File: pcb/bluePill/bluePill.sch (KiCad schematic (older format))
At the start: 6 parts, among them U1 BluePill

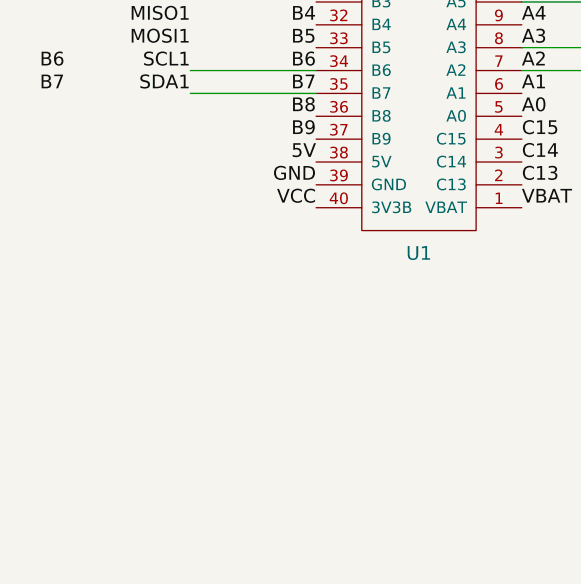
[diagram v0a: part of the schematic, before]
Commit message: Finished the Blue Pill module.
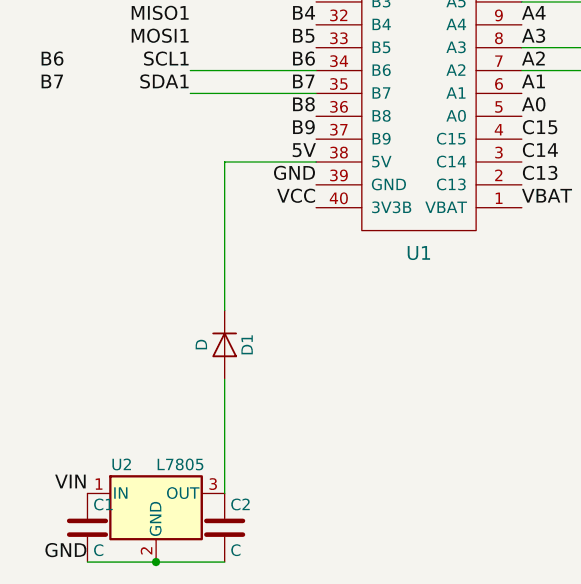
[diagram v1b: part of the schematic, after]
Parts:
- added C1, C2: C, Capacitors_THT:CP_Radial_D6.3mm_P2.50mm, symbol C
- added D1: D, Diodes_THT:D_T-1_P5.08mm_Horizontal, symbol D
- added U2: L7805, Power_Integrations:TO-220, symbol L7805
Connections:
- net 5V: now also D1.1 (K)
- net GND: now also C1.2, C2.2, U2.2 (GND)
- net VIN: now also C1.1, U2.1 (IN)
- new net: C2.1, D1.2 (A), U2.3 (OUT)
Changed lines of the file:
@@
 Text Label 900  1650 2    60   ~ 0
 A9
+$Comp
+L L7805 U2
+U 1 1 5ACA407A
+P 1250 4300
+F 0 "U2" H 1100 4425 50  0000 C CNN
+F 1 "L7805" H 1250 4425 50  0000 L CNN
+F 2 "Power_Integrations:TO-220" H 1275 4150 50  0001 L CIN
+F 3 "" H 1250 4250 50  0001 C CNN
+	1    1250 4300
+	1    0    0    -1
+$EndComp
+$Comp
+L C C1
+U 1 1 5ACA411D
+P 950 4450
+F 0 "C1" H 975 4550 50  0000 L CNN
+F 1 "C" H 975 4350 50  0000 L CNN
+F 2 "Capacitors_THT:CP_Radial_D6.3mm_P2.50mm" H 988 4300 50  0001 C CNN
+F 3 "" H 950 4450 50  0001 C CNN
+	1    950  4450
+	1    0    0    -1
+$EndComp
+$Comp
+L C C2
+U 1 1 5ACA4158
+P 1550 4450
+F 0 "C2" H 1575 4550 50  0000 L CNN
+F 1 "C" H 1575 4350 50  0000 L CNN
+F 2 "Capacitors_THT:CP_Radial_D6.3mm_P2.50mm" H 1588 4300 50  0001 C CNN
+F 3 "" H 1550 4450 50  0001 C CNN
+	1    1550 4450
+	1    0    0    -1
+$EndComp
+Wire Wire Line
+	950  4600 1550 4600
+Connection ~ 1250 4600
+Text Label 950  4300 2    60   ~ 0
+VIN
+Text Label 950  4600 2    60   ~ 0
+GND
+$Comp
+L D D1
+U 1 1 5ACA4326
+P 1550 3650
+F 0 "D1" H 1550 3750 50  0000 C CNN
+F 1 "D" H 1550 3550 50  0000 C CNN
+F 2 "Diodes_THT:D_T-1_P5.08mm_Horizontal" H 1550 3650 50  0001 C CNN
+F 3 "" H 1550 3650 50  0001 C CNN
+	1    1550 3650
+	0    1    1    0
+$EndComp
+Wire Wire Line
+	1550 4300 1550 3800
+Wire Wire Line
+	1550 3500 1550 2850
+Wire Wire Line
+	1550 2850 1950 2850
 $EndSCHEMATC

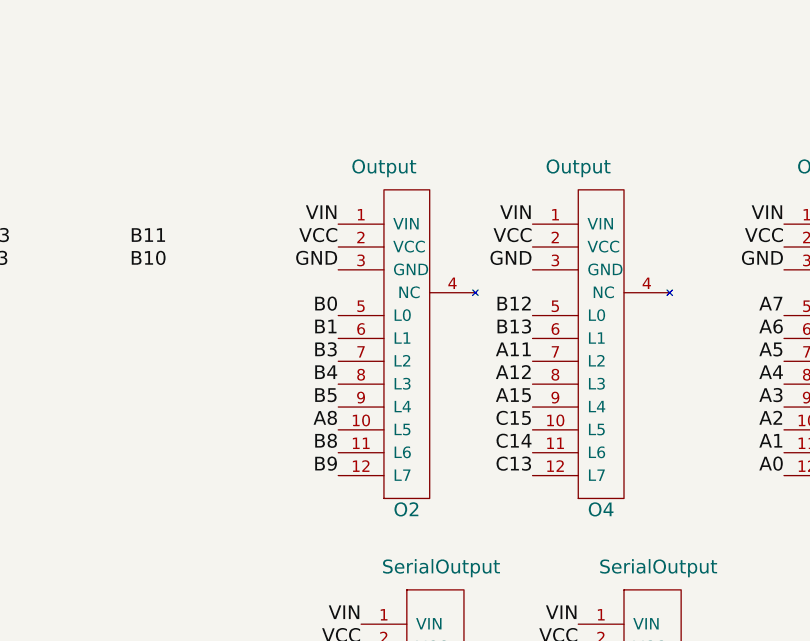
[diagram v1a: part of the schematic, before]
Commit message: "Other" output can have its VCC switched between 5V and 3.3V.
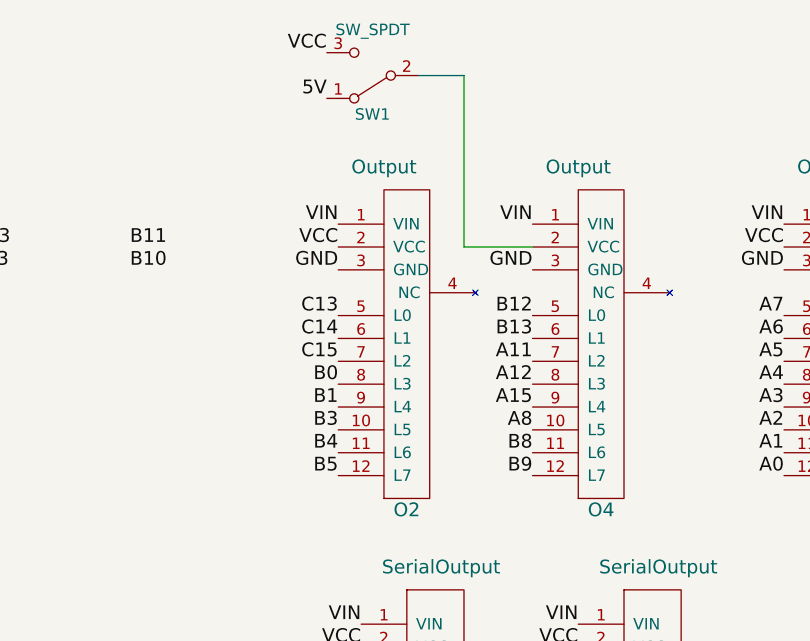
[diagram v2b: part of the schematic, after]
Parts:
- added SW1: SW_SPDT, Pin_Headers:Pin_Header_Straight_1x03_Pitch2.54mm, symbol SW_SPDT
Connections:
- net 5V: now also SW1.1 (A)
- net A8: now also O4.10 (L5); no longer O2.10 (L5)
- net B0: now also O2.8 (L3); no longer O2.5 (L0)
- net B1: now also O2.9 (L4); no longer O2.6 (L1)
- net B3: now also O2.10 (L5); no longer O2.7 (L2)
- net B4: now also O2.11 (L6); no longer O2.8 (L3)
- net B5: now also O2.12 (L7); no longer O2.9 (L4)
- net B8: now also O4.11 (L6); no longer O2.11 (L6)
- net B9: now also O4.12 (L7); no longer O2.12 (L7)
- net C13: now also O2.5 (L0); no longer O4.12 (L7)
- net C14: now also O2.6 (L1); no longer O4.11 (L6)
- net C15: now also O2.7 (L2); no longer O4.10 (L5)
- net VCC: now also SW1.3 (C); no longer O4.2 (VCC)
- new net: O4.2 (VCC), SW1.2 (B)
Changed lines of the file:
@@
 Text Label 5200 1650 2    60   ~ 0
 GND
-Text Label 5200 1850 2    60   ~ 0
+Text Label 5200 2150 2    60   ~ 0
 B0
-Text Label 5200 1950 2    60   ~ 0
+Text Label 5200 2250 2    60   ~ 0
 B1
-Text Label 5200 2450 2    60   ~ 0
+Text Label 6050 2450 2    60   ~ 0
 B8
-Text Label 5200 2550 2    60   ~ 0
+Text Label 6050 2550 2    60   ~ 0
 B9
 Text Label 4450 1650 2    60   ~ 0
@@
 Text Label 6050 1850 2    60   ~ 0
 B12
-Text Label 5200 2350 2    60   ~ 0
+Text Label 6050 2350 2    60   ~ 0
 A8
 Text Label 5300 3200 2    60   ~ 0
@@
 Text Label 6050 2250 2    60   ~ 0
 A15
-Text Label 6050 2350 2    60   ~ 0
+Text Label 5200 2050 2    60   ~ 0
 C15
-Text Label 6050 2450 2    60   ~ 0
+Text Label 5200 1950 2    60   ~ 0
 C14
-Text Label 6050 2550 2    60   ~ 0
+Text Label 5200 1850 2    60   ~ 0
 C13
 Text Label 6050 1450 2    60   ~ 0
 VIN
-Text Label 6050 1550 2    60   ~ 0
+Text Label 5150 700  2    60   ~ 0
 VCC
 Text Label 6050 1650 2    60   ~ 0
 GND
-Text Label 5200 2050 2    60   ~ 0
+Text Label 5200 2350 2    60   ~ 0
 B3
-Text Label 5200 2250 2    60   ~ 0
+Text Label 5200 2550 2    60   ~ 0
 B5
 Text Label 6250 3900 2    60   ~ 0
@@
 Text Label 3600 1650 0    60   ~ 0
 TX3
-Text Label 5200 2150 2    60   ~ 0
+Text Label 5200 2450 2    60   ~ 0
 B4
 Text Label 850  2450 2    60   ~ 0
@@
 Wire Wire Line
 	1550 2850 1950 2850
+$Comp
+L SW_SPDT SW1
+U 1 1 5ACB3745
+P 5350 800
+F 0 "SW1" H 5350 970 50  0000 C CNN
+F 1 "SW_SPDT" H 5350 600 50  0000 C CNN
+F 2 "Pin_Headers:Pin_Header_Straight_1x03_Pitch2.54mm" H 5350 800 50  0001 C CNN
+F 3 "" H 5350 800 50  0001 C CNN
+	1    5350 800
+	-1   0    0    1
+$EndComp
+Text Label 5150 900  2    60   ~ 0
+5V
+Wire Wire Line
+	6050 1550 5750 1550
+Wire Wire Line
+	5750 1550 5750 800
+Wire Wire Line
+	5750 800  5550 800
 $EndSCHEMATC

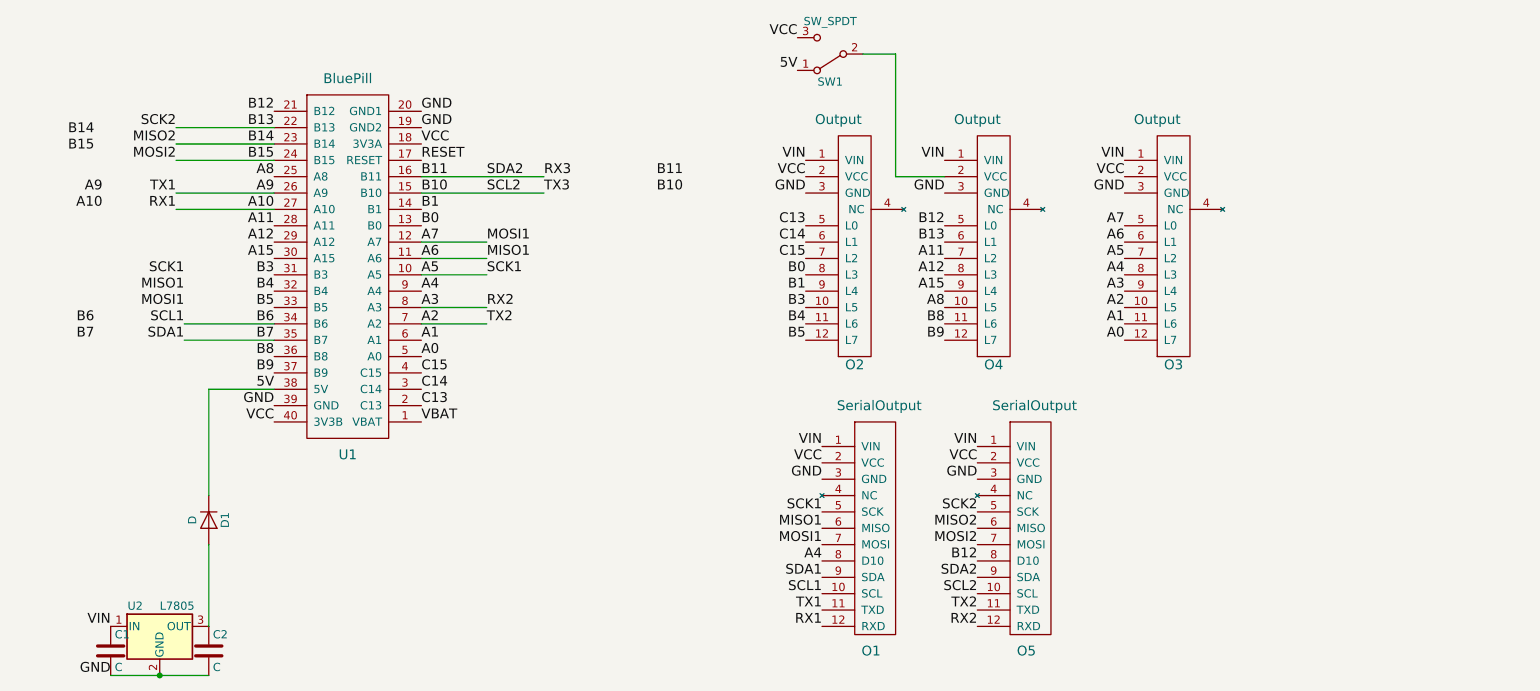
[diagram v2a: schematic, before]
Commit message: Added a Rotary Encoder module. Tidied up a couple of modules before printing them.
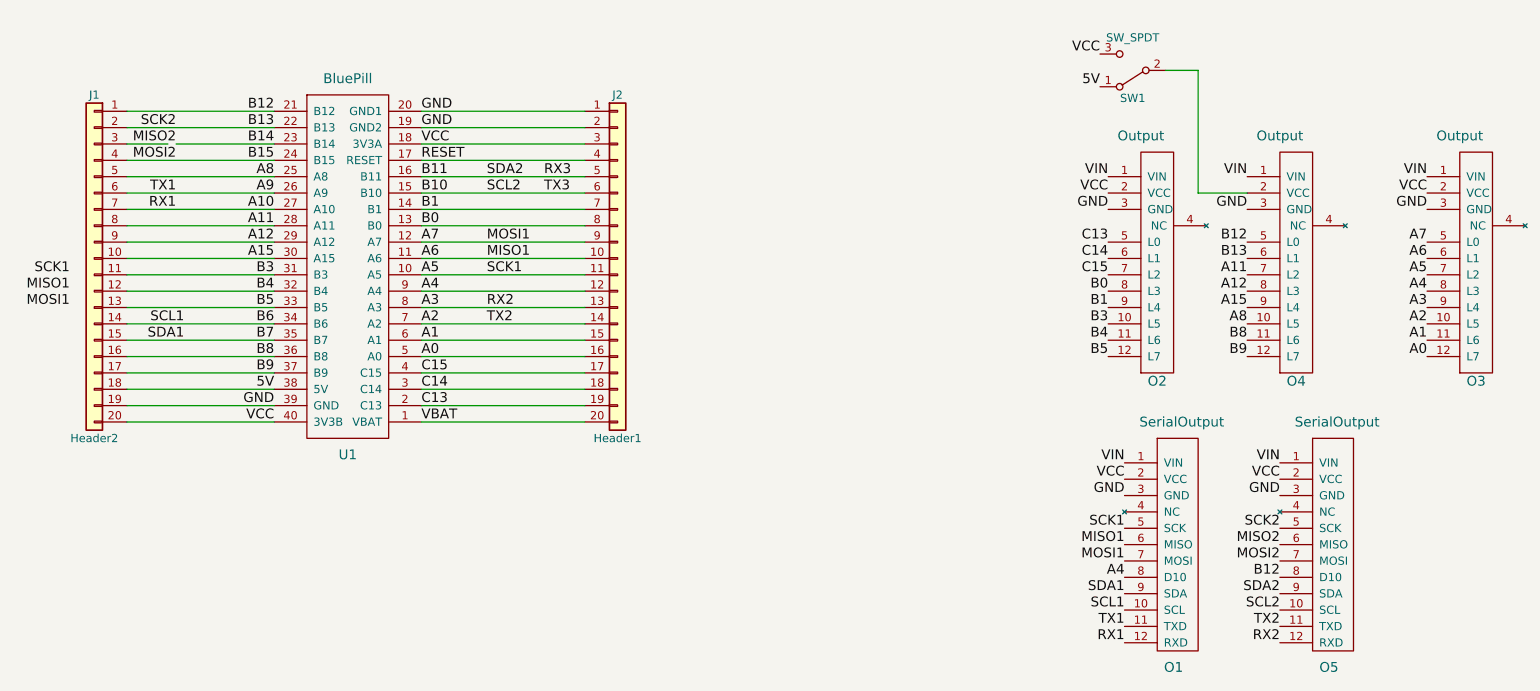
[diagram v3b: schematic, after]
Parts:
- removed C1, C2: C, Capacitors_THT:CP_Radial_D6.3mm_P2.50mm, symbol C
- removed D1: D, Diodes_THT:D_T-1_P5.08mm_Horizontal, symbol D
- removed U2: L7805, Power_Integrations:TO-220, symbol L7805
- added J1: Header2, Pin_Headers:Pin_Header_Straight_1x20_Pitch2.54mm, symbol Conn_01x20
- added J2: Header1, Pin_Headers:Pin_Header_Straight_1x20_Pitch2.54mm, symbol Conn_01x20
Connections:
- net 5V: now also J1.18 (Pin_18)
- net A0: now also J2.16 (Pin_16)
- net A1: now also J2.15 (Pin_15)
- net A10: now also J1.7 (Pin_7)
- net A11: now also J1.8 (Pin_8)
- net A12: now also J1.9 (Pin_9)
- net A15: now also J1.10 (Pin_10)
- net A2: now also J2.14 (Pin_14)
- net A3: now also J2.13 (Pin_13)
- net A4: now also J2.12 (Pin_12)
- net A5: now also J2.11 (Pin_11)
- net A6: now also J2.10 (Pin_10)
- net A7: now also J2.9 (Pin_9)
- net A8: now also J1.5 (Pin_5)
- net A9: now also J1.6 (Pin_6)
- net B0: now also J2.8 (Pin_8)
- net B1: now also J2.7 (Pin_7)
- net B10: now also J2.6 (Pin_6)
- net B11: now also J2.5 (Pin_5)
- net B12: now also J1.1 (Pin_1)
- net B13: now also J1.2 (Pin_2)
- net B15: now also J1.4 (Pin_4)
- net B3: now also J1.11 (Pin_11)
- net B4: now also J1.12 (Pin_12)
- net B5: now also J1.13 (Pin_13)
- net B6: now also J1.14 (Pin_14)
- net B7: now also J1.15 (Pin_15)
- net B8: now also J1.16 (Pin_16)
- net B9: now also J1.17 (Pin_17)
- net C13: now also J2.19 (Pin_19)
- net C14: now also J2.18 (Pin_18)
- net C15: now also J2.17 (Pin_17)
- net GND: now also J1.19 (Pin_19), J2.1 (Pin_1), J2.2 (Pin_2)
- net RESET: now also J2.4 (Pin_4)
- net VBAT: now also J2.20 (Pin_20)
- net VCC: now also J1.20 (Pin_20), J2.3 (Pin_3)
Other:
- moved on the sheet: O1, O2, O3, O4, O5, SW1

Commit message: Ready for the second batch of PCBs to be printed.
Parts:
- removed SW1: SW_SPDT, Pin_Headers:Pin_Header_Straight_1x03_Pitch2.54mm, symbol SW_SPDT
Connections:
- net VCC: now also O4.2 (VCC)
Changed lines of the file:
@@
 Text Label 7900 1550 2    60   ~ 0
 VIN
-Text Label 7000 800  2    60   ~ 0
-VCC
 Text Label 7900 1750 2    60   ~ 0
 GND
@@
 Text Label 7900 2050 2    60   ~ 0
 B13
-$Comp
-L SW_SPDT SW1
-U 1 1 5ACB3745
-P 7200 900
-F 0 "SW1" H 7200 1070 50  0000 C CNN
-F 1 "SW_SPDT" H 7200 700 50  0000 C CNN
-F 2 "Pin_Headers:Pin_Header_Straight_1x03_Pitch2.54mm" H 7200 900 50  0001 C CNN
-F 3 "" H 7200 900 50  0001 C CNN
-	1    7200 900
-	-1   0    0    1
-$EndComp
-Text Label 7000 1000 2    60   ~ 0
-5V
-Wire Wire Line
-	7900 1650 7600 1650
-Wire Wire Line
-	7600 1650 7600 900
-Wire Wire Line
-	7600 900  7400 900
 $Comp
 L Conn_01x20 J2
@@
 Wire Wire Line
 	1050 3050 1950 3050
+Text Label 7900 1650 2    60   ~ 0
+VCC
 $EndSCHEMATC

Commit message: Added README.md for each of the modules, plus a few minor tweaks to PCB layouts while writing the text.
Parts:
- added J3: Power, Pin_Headers:Pin_Header_Straight_1x05_Pitch2.54mm, symbol Conn_01x05
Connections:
- net 5V: now also J3.1 (Pin_1)
- net GND: now also J3.4 (Pin_4)
- net RESET: now also J3.5 (Pin_5)
- net VBAT: now also J3.2 (Pin_2)
- net VCC: now also J3.3 (Pin_3)
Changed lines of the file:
@@
 Text Label 7900 1650 2    60   ~ 0
 VCC
+Text Label 5100 3350 2    60   ~ 0
+VBAT
+Text Label 5100 3250 2    60   ~ 0
+5V
+Text Label 5100 3650 2    60   ~ 0
+RESET
+Text Label 5100 3450 2    60   ~ 0
+VCC
+Text Label 5100 3550 2    60   ~ 0
+GND
+$Comp
+L Conn_01x05 J3
+U 1 1 5AFAA468
+P 5300 3450
+F 0 "J3" H 5300 3750 50  0000 C CNN
+F 1 "Power" H 5300 3150 50  0000 C CNN
+F 2 "Pin_Headers:Pin_Header_Straight_1x05_Pitch2.54mm" H 5300 3450 50  0001 C CNN
+F 3 "" H 5300 3450 50  0001 C CNN
+	1    5300 3450
+	1    0    0    -1
+$EndComp
 $EndSCHEMATC
